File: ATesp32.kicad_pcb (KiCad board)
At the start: 4 copper layers, 18 x 51.2 mm, 51 parts, among them J1 USB_C_Receptacle_USB2.0_16P, J2 JST PH, Q1 DMP2045U, SW1 SW_Push, SW2 SW_Push, U1 ESP32-S3, U2 ATmega32A-P, U3 MCP73831-2-OT, U4 AP2112K-3.3, U5 CP2102N-Axx-xQFN24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

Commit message: cleanup
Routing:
- net GND: track 15.4 -> 14.3 mm
- net PD4: track 3.26 -> 2.19 mm
- net PA2: track 29.7 -> 29.1 mm
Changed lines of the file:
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@@
 	)
 	(segment
-		(start 79.0125 55.7125)
-		(end 79.025 55.7)
-		(width 0.355542)
-		(layer "F.Cu")
-		(net 1)
-	)
-	(segment
 		(start 79.8 54)
 		(end 79.3 54.5)
@@
 	)
 	(segment
-		(start 83.25 90.9125)
-		(end 84 90.1625)
-		(width 0.25)
-		(layer "F.Cu")
-		(net 3)
-	)
-	(segment
 		(start 83.25 92.1)
 		(end 83.25 92.732108)
@@
 	)
 	(segment
-		(start 80.5 55.775)
-		(end 80.525 55.75)
-		(width 0.355542)
-		(layer "F.Cu")
-		(net 3)
-	)
-	(segment
 		(start 80.28 94.88)
 		(end 79.68 95.48)
@@
 	)
 	(segment
-		(start 87.390488 77.839411)
-		(end 87.660589 77.839411)
-		(width 0.15)
-		(layer "F.Cu")
-		(net 5)
-	)
-	(segment
-		(start 79.439411 82.639411)
-		(end 79.439411 82.660589)
-		(width 0.5)
-		(layer "F.Cu")
-		(net 5)
-	)
-	(segment
 		(start 80.039411 74.060589)
 		(end 79.628822 73.65)
@@
 	)
 	(segment
-		(start 80.575 57.3125)
-		(end 80.5875 57.3)
-		(width 0.355542)
-		(layer "F.Cu")
-		(net 7)
-	)
-	(segment
 		(start 80.575 58.8)
 		(end 81.7 59.925)
@@
 	)
 	(segment
-		(start 78.6 65.890001)
-		(end 78.490001 66)
-		(width 0.15)
-		(layer "F.Cu")
-		(net 8)
-	)
-	(segment
-		(start 78.490001 66.970001)
-		(end 78.52 67)
-		(width 0.15)
-		(layer "F.Cu")
-		(net 8)
-	)
-	(segment
 		(start 78.6 60.45)
 		(end 78.6 64.55)
@@
 	)
 	(segment
-		(start 84.324991 94.954991)
-		(end 84.25 94.88)
-		(width 0.15)
-		(layer "F.Cu")
-		(net 16)
-	)
-	(segment
 		(start 84.25 93.949999)
 		(end 84.2 93.899999)
@@
 	)
 	(segment
-		(start 83.25 94.88)
-		(end 83.175 94.955)
-		(width 0.15)
-		(layer "F.Cu")
-		(net 16)
-	)
-	(segment
 		(start 84.25 95.775)
 		(end 84.25 94.88)
@@
 	)
 	(segment
-		(start 82.75 93.26)
-		(end 82.76 93.25)
-		(width 0.15)
-		(layer "F.Cu")
-		(net 18)
-	)
-	(segment
 		(start 82.75 94.88)
 		(end 82.75 93.26)
@@
 	)
 	(segment
-		(start 76.38 94.55)
-		(end 76.95 94.55)
-		(width 0.15)
-		(layer "B.Cu")
-		(net 21)
-	)
-	(segment
 		(start 76.95 94.55)
 		(end 78.5 93)
@@
 	)
 	(segment
-		(start 78.5 93)
-		(end 79 93)
-		(width 0.15)
-		(layer "B.Cu")
-		(net 21)
-	)
-	(segment
 		(start 78.6 69.9125)
 		(end 78.6 68.35)
@@
 		(net 26)
 	)
-	(segment
-		(start 82.05 89.9)
-		(end 82.0625 89.9125)
-		(width 0.15)
-		(layer "F.Cu")
-		(net 26)
-	)
 	(via
 		(at 81 89.9)
@@
 	)
 	(segment
-		(start 79.25 89.9)
-		(end 79 89.65)
-		(width 0.15)
-		(layer "B.Cu")
-		(net 26)
-	)
-	(segment
 		(start 81 89.9)
 		(end 79.25 89.9)
@@
 	)
 	(segment
-		(start 81.65 87)
-		(end 81.5 87.15)
-		(width 0.15)
-		(layer "B.Cu")
-		(net 27)
-	)
-	(segment
 		(start 81.5 89.4)
 		(end 82.05 89.4)
@@
 		(net 28)
 	)
-	(segment
-		(start 82.05 89.4)
-		(end 82.0625 89.4125)
-		(width 0.15)
-		(layer "F.Cu")
-		(net 28)
-	)
 	(via
 		(at 81.5 89.4)
@@
 	)
 	(segment
-		(start 88.75 63.963172)
-		(end 88.75 63.775)
-		(width 0.25)
-		(layer "F.Cu")
-		(net 29)
-	)
-	(segment
 		(start 88.76 69.5)
 		(end 88.76 68.035)
@@
 	)
 	(segment
-		(start 88.76 68.035)
-		(end 88.75 68.025)
-		(width 0.5)
-		(layer "F.Cu")
-		(net 30)
-	)
-	(segment
 		(start 85.50496 78.330518)
 		(end 85.50496 78.063238)
@@
 	)
 	(segment
-		(start 84.1 86.99)
-		(end 84.11 87)
-		(width 0.15)
-		(layer "F.Cu")
-		(net 31)
-	)
-	(segment
 		(start 85.75 78.575558)
 		(end 85.50496 78.330518)
@@
 	)
 	(segment
-		(start 85.83094 77.737258)
-		(end 85.83094 77.701903)
-		(width 0.15)
-		(layer "F.Cu")
-		(net 31)
-	)
-	(segment
 		(start 84.1 86.3)
 		(end 84.1 86.99)
@@
 	)
 	(segment
-		(start 84.75 86.14)
-		(end 84.89 86)
-		(width 0.25)
-		(layer "F.Cu")
-		(net 34)
-	)
-	(segment
 		(start 84.75 88.225)
 		(end 84.75 86.14)
@@
 	)
 	(segment
-		(start 85.25 87.14)
-		(end 85.39 87)
-		(width 0.25)
-		(layer "F.Cu")
-		(net 35)
-	)
-	(segment
 		(start 85.25 88.225)
 		(end 85.25 87.14)
@@
 	)
 	(segment
-		(start 78.972004 79.398959)
-		(end 78.936647 79.398959)
-		(width 0.15)
-		(layer "F.Cu")
-		(net 36)
-	)
-	(segment
 		(start 78.936647 79.398959)
 		(end 78.568844 79.031156)
@@
 	)
 	(segment
-		(start 91.036827 56.45)
-		(end 91.62 56.45)
-		(width 0.15)
-		(layer "B.Cu")
-		(net 36)
-	)
-	(segment
 		(start 86.6 72.349098)
 		(end 86.6 60.886827)
@@
 	)
 	(segment
-		(start 80.636898 77.701903)
-		(end 80.66906 77.701903)
-		(width 0.15)
-		(layer "F.Cu")
-		(net 38)
-	)
-	(segment
 		(start 79.990524 77.161596)
 		(end 80.096591 77.161596)
@@
 	)
 	(segment
-		(start 76.413173 56.45)
-		(end 76.38 56.45)
-		(width 0.15)
-		(layer "B.Cu")
-		(net 38)
-	)
-	(segment
 		(start 78.75 72.798959)
 		(end 78.75 58.786827)
@@
 	)
 	(segment
-		(start 91.531041 79.398959)
-		(end 91.62 79.31)
-		(width 0.15)
-		(layer "F.Cu")
-		(net 43)
-	)
-	(segment
 		(start 78.670867 78.532137)
 		(end 79.254847 79.116117)
@@
 	)
 	(segment
-		(start 91.62 61.53)
-		(end 91.468959 61.53)
-		(width 0.15)
-		(layer "B.Cu")
-		(net 46)
-	)
-	(segment
 		(start 91.468959 61.53)
 		(end 88.825 64.173959)
@@
 	)
 	(segment
-		(start 76.38 89.380228)
-		(end 76.38 89.47)
-		(width 0.15)
-		(layer "B.Cu")
-		(net 69)
-	)
-	(segment
-		(start 79.502334 78.833274)
-		(end 79.537689 78.833274)
-		(width 0.15)
-		(layer "F.Cu")
-		(net 70)
-	)
-	(segment
 		(start 78.68453 78.01547)
 		(end 79.502334 78.833274)
@@
 	)
 	(segment
-		(start 85.977207 73.823223)
-		(end 86.121142 73.823223)
-		(width 0.15)
-		(layer "F.Cu")
-		(net 92)
-	)
-	(segment
 		(start 88.8617 74.159619)
 		(end 87.4818 74.159619)
@@
 	)
 	(segment
-		(start 88.878858 73.967158)
-		(end 88.878858 74.176777)
-		(width 0.15)
-		(layer "F.Cu")
-		(net 93)
-	)
-	(segment
 		(start 86.020101 75.25)
 		(end 84.699569 76.570532)
 		(width 0.2)
 		(layer "F.Cu")
-		(net 93)
-	)
-	(segment
-		(start 88.878858 74.176777)
-		(end 88.8617 74.159619)
-		(width 0.2)
-		(layer "F.Cu")

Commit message: fix silk
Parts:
- C8, C9: footprint Capacitor_SMD:C_0603_1608Metric -> Capacitor_SMD:C_0402_1005Metric
- L2: footprint Inductor_SMD:L_0603_1608Metric -> Inductor_SMD:L_0402_1005Metric
- SW1: value SW_Push -> RESET
- SW2: value SW_Push -> BOOT
- moved L2 0.55 mm to (80.3, 57.2), turned to 90 degrees
- moved C8 0.10 mm to (79.9, 58.8)
- moved C9 0.10 mm to (79.9, 55.7), turned to 180 degrees
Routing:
- net GND: track 14.3 -> 12.4 mm, vias 68 -> 70
- net Net-(AE1-PCB_Trace): track 3.61 -> 3.02 mm
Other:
- board text added: "+"
- board text added: "-"

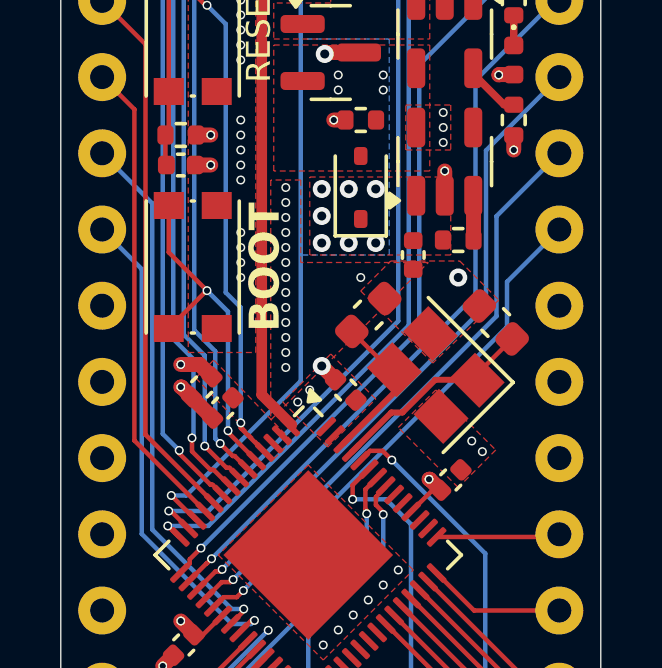
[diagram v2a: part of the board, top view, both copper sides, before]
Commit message: move crystal farther from chip
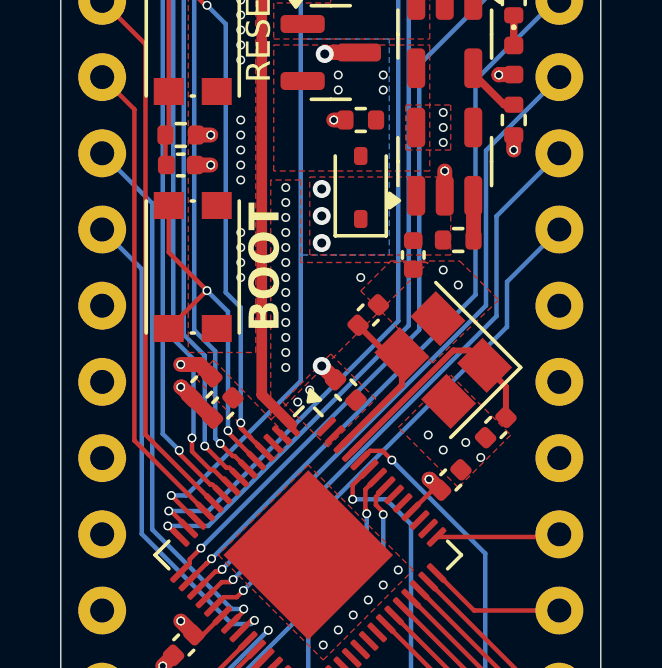
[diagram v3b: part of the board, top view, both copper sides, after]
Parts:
- C11, C12: footprint Capacitor_SMD:C_0603_1608Metric -> Capacitor_SMD:C_0402_1005Metric
- moved C12 3.50 mm to (89.5, 75.8), turned to -135 degrees
- moved Y1 0.56 mm to (87.8, 73.5)
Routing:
- net XTAL_N: track 6.81 -> 8.31 mm
- net XTAL_P: track 4.97 -> 5.64 mm
- net Net-(D4-K): vias 8 -> 4
- net GND: vias 70 -> 73

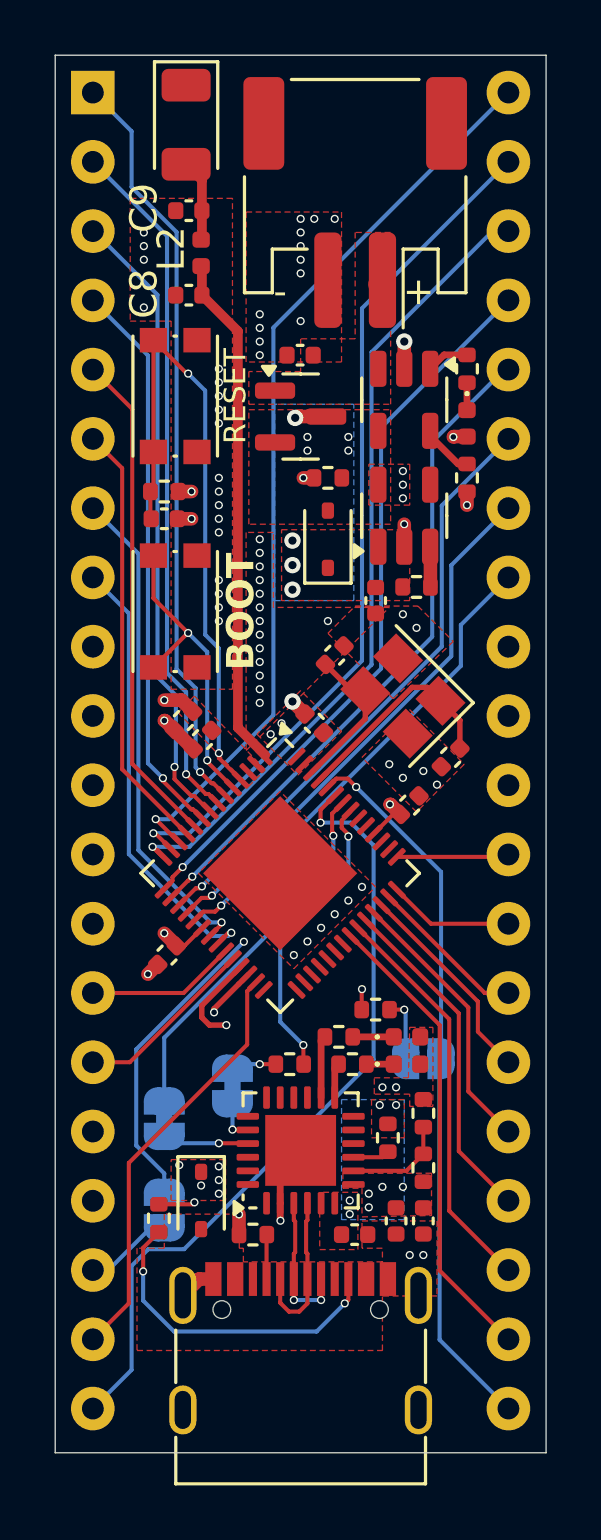
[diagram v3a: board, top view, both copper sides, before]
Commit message: critical error - changed to correct mosfet pin numbers
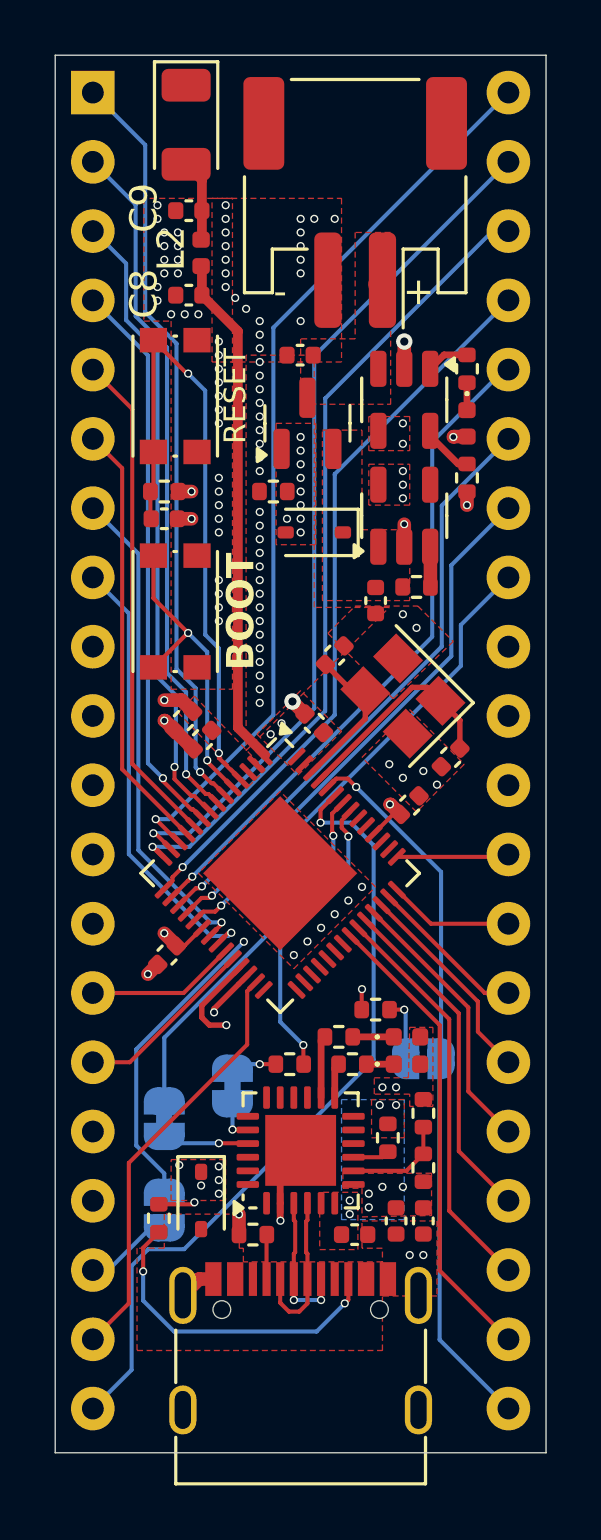
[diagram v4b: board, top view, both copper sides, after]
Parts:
- moved R2 2.06 mm to (83.0, 66.0)
- moved D4 0.56 mm to (84.5, 67.5), turned to 180 degrees
- moved Q1 0.35 mm to (84.2, 63.5), turned to 90 degrees
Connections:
- Q1 pad 1: +BATT -> +5V
- Q1 pad 2: +5V -> Net-(D4-K)
- Q1 pad 3: Net-(D4-K) -> +BATT
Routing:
- net Net-(D4-K): track 1.16 -> 0.00 mm, vias 4 -> 0
- net GND: track 12.4 -> 12.0 mm, vias 73 -> 103
- net +5V: vias 13 -> 20
- removed copper zone on B.Cu, net Net-(D4-K)

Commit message: antenna was backwards
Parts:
- moved R2 0.75 mm to (83.8, 66.0)
- turned AE1 to 90 degrees
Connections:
- AE1 pad 1: unconnected-(AE1-FEED-Pad1) -> Net-(AE1-FEED)
- AE1 pad 2: Net-(AE1-PCB_Trace) -> unconnected-(AE1-PCB_Trace-Pad2)
- C9 pad 1: Net-(AE1-PCB_Trace) -> Net-(AE1-FEED)
- L2 pad 2: Net-(AE1-PCB_Trace) -> Net-(AE1-FEED)
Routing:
- net Net-(AE1-PCB_Trace): track 3.02 -> 0.00 mm
- net Net-(AE1-FEED): track 0.00 -> 3.02 mm
- net GND: vias 103 -> 105
- net +5V: vias 20 -> 17
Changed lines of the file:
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@@
 	)
 	(net 0 "")
-	(net 1 "Net-(AE1-PCB_Trace)")
-	(net 2 "unconnected-(AE1-FEED-Pad1)")
+	(net 1 "unconnected-(AE1-PCB_Trace-Pad2)")
+	(net 2 "Net-(AE1-FEED)")
 	(net 3 "GND")
 	(net 4 "Net-(D4-K)")
@@
 			(layers "F.Cu" "F.Paste" "F.Mask")
 			(roundrect_rratio 0.25)
-			(net 1 "Net-(AE1-PCB_Trace)")
+			(net 2 "Net-(AE1-FEED)")
 			(pintype "passive")
 		)
@@
 		)
 		(property "Value" "RESET"
-			(at 0 -2.2 90)
+			(at 0 -2.4 90)
 			(layer "F.SilkS")
 			(effects
 				(font
-					(size 0.8 0.8)
+					(size 1 1)
 					(thickness 0.15)
 				)
@@
 	(footprint "Resistor_SMD:R_0402_1005Metric"
 		(layer "F.Cu")
-		(at 83 66)
+		(at 83.75 66)
 		(descr "Resistor SMD 0402 (1005 Metric), square (rectangular) end terminal, IPC_7351 nominal, (Body size source: IPC-SM-782 page 72, https://www.pcb-3d.com/wordpress/wp-content/uploads/ipc-sm-782a_amendment_1_and_2.pdf), generated with kicad-footprint-generator")
 		(tags "resistor")
@@
 	(footprint "RF_Antenna:Johanson_2450AT18x100"
 		(layer "F.Cu")
-		(at 79.8 52.55 -90)
+		(at 79.8 52.55 90)
 		(descr "Johanson 2450AT43F0100 SMD antenna 2400-2500Mhz, -0.5dBi, https://www.johansontechnology.com/datasheets/2450AT18A100/2450AT18A100.pdf")
 		(tags "antenna")
@@
 		)
 		(property "Footprint" "RF_Antenna:Johanson_2450AT18x100"
-			(at 0 0 -90)
+			(at 0 0 90)
 			(unlocked yes)
 			(layer "F.Fab")
@@
 		)
 		(property "Datasheet" ""
-			(at 0 0 -90)
+			(at 0 0 90)
 			(unlocked yes)
 			(layer "F.Fab")
@@
 		)
 		(property "Description" "Ceramic chip antenna with pin for PCB trace"
-			(at 0 0 -90)
+			(at 0 0 90)
 			(unlocked yes)
 			(layer "F.Fab")
@@
 		)
 		(property "DigiKey" "712-2450AT18B0100001ECT-ND"
-			(at 0 0 -90)
+			(at 0 0 90)
 			(unlocked yes)
 			(layer "F.Fab")
@@
 		(attr smd)
 		(fp_line
-			(start -2.31 1.16)
-			(end 1.6 1.16)
+			(start 1.6 -1.16)
+			(end -2.31 -1.16)
 			(stroke
 				(width 0.12)
@@
 		)
 		(fp_line
-			(start 1.6 -1.16)
-			(end -2.31 -1.16)
+			(start -2.31 1.16)
+			(end 1.6 1.16)
 			(stroke
 				(width 0.12)
@@
 		)
 		(fp_line
-			(start -2.3 1.15)
-			(end -2.3 -1.15)
+			(start 2.3 -1.15)
+			(end 2.3 1.15)
 			(stroke
 				(width 0.05)
@@
 		)
 		(fp_line
-			(start 2.3 1.15)
-			(end -2.3 1.15)
+			(start -2.3 -1.15)
+			(end 2.3 -1.15)
 			(stroke
 				(width 0.05)
@@
 		)
 		(fp_line
-			(start -2.3 -1.15)
-			(end 2.3 -1.15)
+			(start 2.3 1.15)
+			(end -2.3 1.15)
 			(stroke
 				(width 0.05)
@@
 		)
 		(fp_line
-			(start 2.3 -1.15)
-			(end 2.3 1.15)
+			(start -2.3 1.15)
+			(end -2.3 -1.15)
 			(stroke
 				(width 0.05)
@@
 		)
 		(fp_line
-			(start -1.6 0.8)
-			(end 1.6 0.8)
+			(start 1.6 -0.8)
+			(end -1.2 -0.8)
 			(stroke
 				(width 0.1)
@@
 		)
 		(fp_line
-			(start 1.6 0.8)
-			(end 1.6 -0.8)
+			(start -1.2 -0.8)
+			(end -1.6 -0.4)
 			(stroke
 				(width 0.1)
@@
 		)
 		(fp_line
-			(start -1.2 -0.8)
-			(end -1.6 -0.4)
+			(start 1.6 0.8)
+			(end 1.6 -0.8)
 			(stroke
 				(width 0.1)
@@
 		)
 		(fp_line
-			(start 1.6 -0.8)
-			(end -1.2 -0.8)
+			(start -1.6 0.8)
+			(end 1.6 0.8)
 			(stroke
 				(width 0.1)
@@
 		)
 		(pad "1" smd roundrect
-			(at -1.45 0 270)
+			(at -1.45 0 90)
 			(size 1.2 1.8)
 			(layers "F.Cu" "F.Paste" "F.Mask")
 			(roundrect_rratio 0.208333)
-			(net 2 "unconnected-(AE1-FEED-Pad1)")
+			(net 2 "Net-(AE1-FEED)")
 			(pinfunction "FEED")
-			(pintype "input+no_connect")
+			(pintype "input")
 		)
 		(pad "2" smd roundrect
-			(at 1.45 0 270)
+			(at 1.45 0 90)
 			(size 1.2 1.8)
 			(layers "F.Cu" "F.Paste" "F.Mask")
 			(roundrect_rratio 0.208333)
-			(net 1 "Net-(AE1-PCB_Trace)")
+			(net 1 "unconnected-(AE1-PCB_Trace-Pad2)")
 			(pinfunction "PCB_Trace")
-			(pintype "passive")
+			(pintype "passive+no_connect")
 		)
 		(model "${KICAD8_3DMODEL_DIR}/RF_Antenna.3dshapes/Johanson_2450AT18x100.wrl"
@@
 			(layers "F.Cu" "F.Paste" "F.Mask")
 			(roundrect_rratio 0.25)
-			(net 1 "Net-(AE1-PCB_Trace)")
+			(net 2 "Net-(AE1-FEED)")
 			(pintype "passive")
 		)
@@
 		(width 0.355542)
 		(layer "F.Cu")
-		(net 1)
+		(net 2)
 	)
 	(segment
@@
 		(width 0.355542)
 		(layer "F.Cu")
-		(net 1)
+		(net 2)
 	)
 	(segment
@@
 		(width 0.355542)
 		(layer "F.Cu")
-		(net 1)
+		(net 2)
 	)
 	(segment
@@
 		(width 0.355542)
 		(layer "F.Cu")
-		(net 1)
+		(net 2)
 	)
 	(segment
@@
 	)
 	(via
+		(at 82.5 65.75)
+		(size 0.3)
+		(drill 0.2)
+		(layers "F.Cu" "B.Cu")
+		(free yes)
+		(net 3)
+	)
+	(via
 		(at 81 69.25)
 		(size 0.3)
@@
 	)
 	(via
+		(at 82.5 66.25)
+		(size 0.3)
+		(drill 0.2)
+		(layers "F.Cu" "B.Cu")
+		(free yes)
+		(net 3)
+	)
+	(via
 		(at 78.75 59)
 		(size 0.3)
@@
 	)
 	(via
-		(at 84 66.5)
-		(size 0.3)
-		(drill 0.2)
-		(layers "F.Cu" "B.Cu")
-		(free yes)
-		(net 6)
-	)
-	(via
 		(at 84 67)
 		(size 0.3)
@@
 	)
 	(via
-		(at 84 66)
-		(size 0.3)
-		(drill 0.2)
-		(layers "F.Cu" "B.Cu")
-		(free yes)
-		(net 6)
-	)
-	(via
 		(at 84 64.5)
 		(size 0.3)
@@
 	)
 	(via
-		(at 84 65.5)
-		(size 0.3)
-		(drill 0.2)
-		(layers "F.Cu" "B.Cu")
-		(free yes)
-		(net 6)
-	)
-	(via
 		(at 83.5 67)
 		(size 0.3)
@@
 		(polygon
 			(pts
-				(xy 86 56.5) (xy 86 60.4) (xy 84 60.4) (xy 84 62.8) (xy 87.3 62.8) (xy 87.3 56.5)
+				(xy 86 56.5) (xy 86 60.4) (xy 84 60.4) (xy 84 63.2) (xy 87.3 63.2) (xy 87.3 56.5)
 			)
 		)
@@
 		(polygon
 			(pts
-				(xy 84.8 63.75) (xy 86.25 63.75) (xy 86.25 67.4) (xy 88 67.4) (xy 88 70) (xy 84.8 70)
+				(xy 84.8 63.65) (xy 86.25 63.65) (xy 86.25 67.4) (xy 88 67.4) (xy 88 70) (xy 84.8 70)
 			)
 		)

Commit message: cleanup
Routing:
- net XTAL_N: track 8.31 -> 7.21 mm
- net GND: vias 105 -> 108
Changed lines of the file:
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@@
 		(tags "capacitor")
 		(property "Reference" "C9"
-			(at 1.65 0.1 90)
+			(at 1.65 -0.05 90)
 			(layer "F.SilkS")
 			(effects
@@
 	)
 	(segment
-		(start 80.38 56.735)
-		(end 80.35 56.765)
-		(width 0.355542)
-		(layer "F.Cu")
-		(net 2)
-	)
-	(segment
 		(start 80.38 55.7)
 		(end 80.38 56.735)
@@
 	)
 	(via
+		(at 86.75 71.25)
+		(size 0.3)
+		(drill 0.2)
+		(layers "F.Cu" "B.Cu")
+		(free yes)
+		(net 3)
+	)
+	(via
 		(at 81 62)
 		(size 0.3)
@@
 	)
 	(via
+		(at 86.25 71.25)
+		(size 0.3)
+		(drill 0.2)
+		(layers "F.Cu" "B.Cu")
+		(free yes)
+		(net 3)
+	)
+	(via
 		(at 78.75 59)
 		(size 0.3)
@@
 	)
 	(via
+		(at 85.75 70.75)
+		(size 0.3)
+		(drill 0.2)
+		(layers "F.Cu" "B.Cu")
+		(free yes)
+		(net 3)
+	)
+	(via
 		(at 82.5 62.25)
 		(size 0.3)
@@
 	)
 	(segment
-		(start 80.38 57.765)
-		(end 80.35 57.735)
-		(width 0.355542)
-		(layer "F.Cu")
-		(net 7)
-	)
-	(segment
 		(start 80.38 58.8)
 		(end 80.38 57.765)
@@
 	(segment
 		(start 86.371142 73.323223)
-		(end 85.894401 73.323223)
-		(width 0.2)
-		(layer "F.Cu")
-		(net 92)
-	)
-	(segment
-		(start 86.371142 73.323223)
 		(end 86.371142 74.333273)
 		(width 0.2)
@@
 	)
 	(segment
-		(start 88.633883 73.181802)
-		(end 88.088299 73.181802)
-		(width 0.2)
-		(layer "F.Cu")
-		(net 93)
-	)
-	(segment
-		(start 89.128858 73.676777)
-		(end 89.128858 73.892461)
-		(width 0.2)
-		(layer "F.Cu")
-		(net 93)
-	)
-	(segment
-		(start 88.088299 73.181802)
+		(start 87.670101 73.6)
 		(end 84.699569 76.570532)
 		(width 0.2)
@@
 	)
 	(segment
-		(start 89.128858 73.892461)
-		(end 89.1117 73.909619)
+		(start 89.128858 74.428858)
+		(end 89.128858 73.676777)
 		(width 0.2)
 		(layer "F.Cu")
@@
 	)
 	(segment
-		(start 89.128858 73.676777)
-		(end 88.633883 73.181802)
+		(start 89.839411 75.410589)
+		(end 89.839411 75.139411)
 		(width 0.2)
 		(layer "F.Cu")
@@
 	)
 	(segment
-		(start 89.839411 75.410589)
-		(end 89.839411 74.38733)
+		(start 88.652081 73.6)
+		(end 87.670101 73.6)
 		(width 0.2)
 		(layer "F.Cu")
@@
 	)
 	(segment
-		(start 89.839411 74.38733)
-		(end 89.128858 73.676777)
+		(start 89.839411 75.139411)
+		(end 89.128858 74.428858)
 		(width 0.2)
 		(layer "F.Cu")
